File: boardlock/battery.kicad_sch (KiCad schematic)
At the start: 20 parts, among them J1 Conn_01x02, J2 Conn_01x02, U4 BQ27441DRZR-G1A, U5 BQ24075RGT

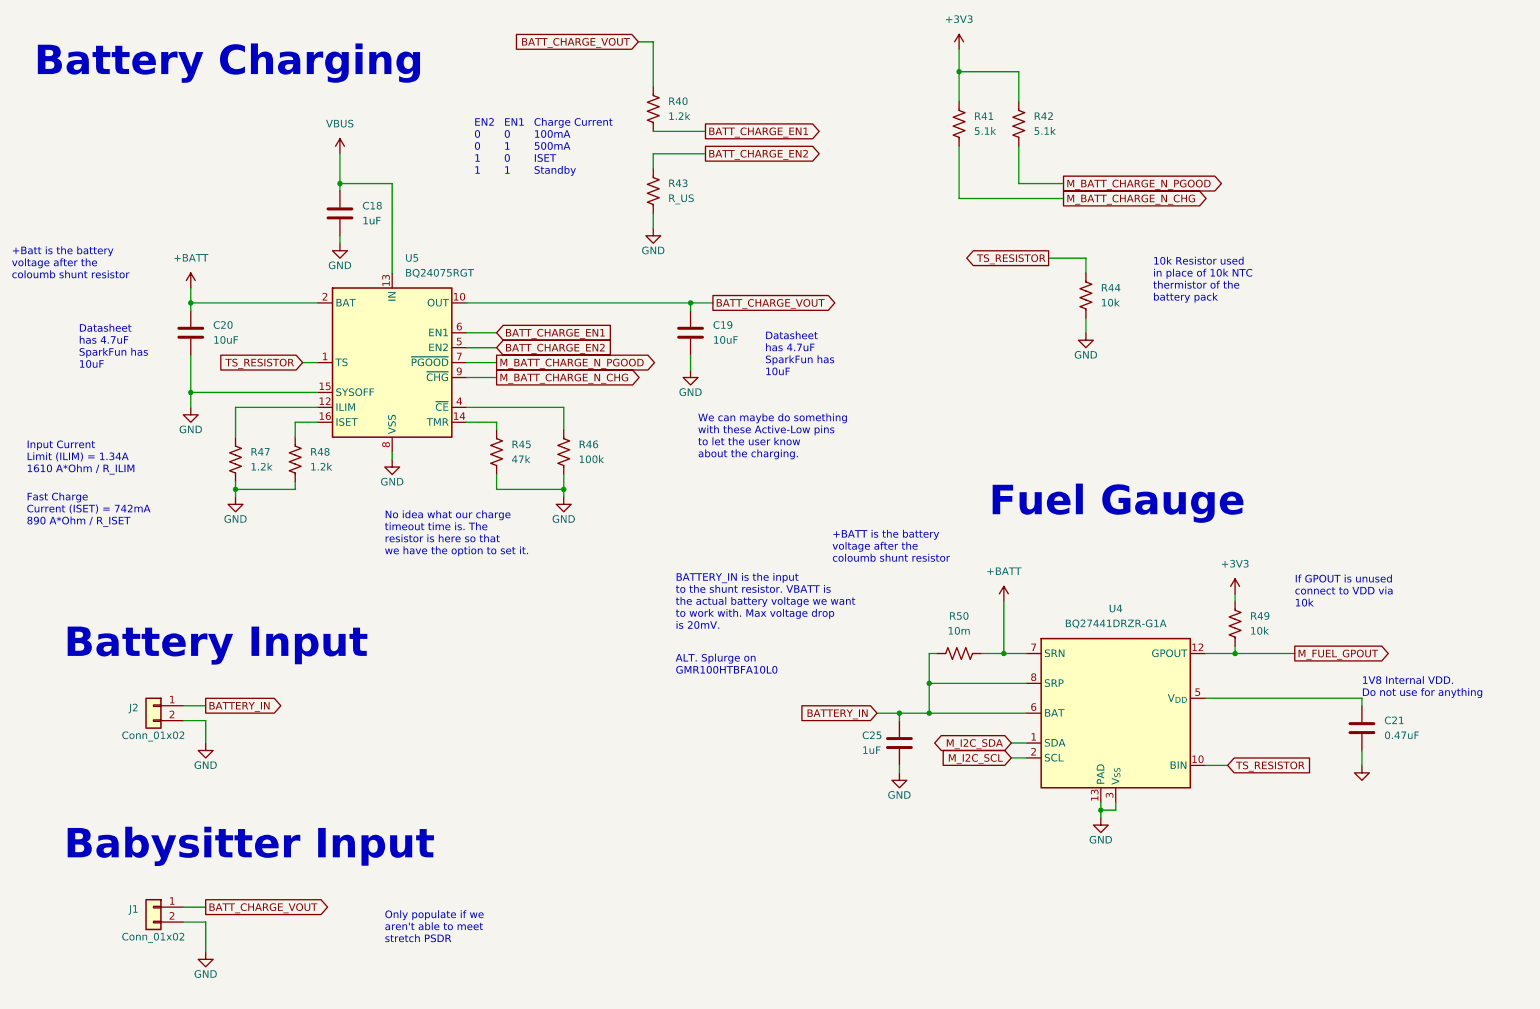
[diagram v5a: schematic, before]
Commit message: Repositioned USB C port
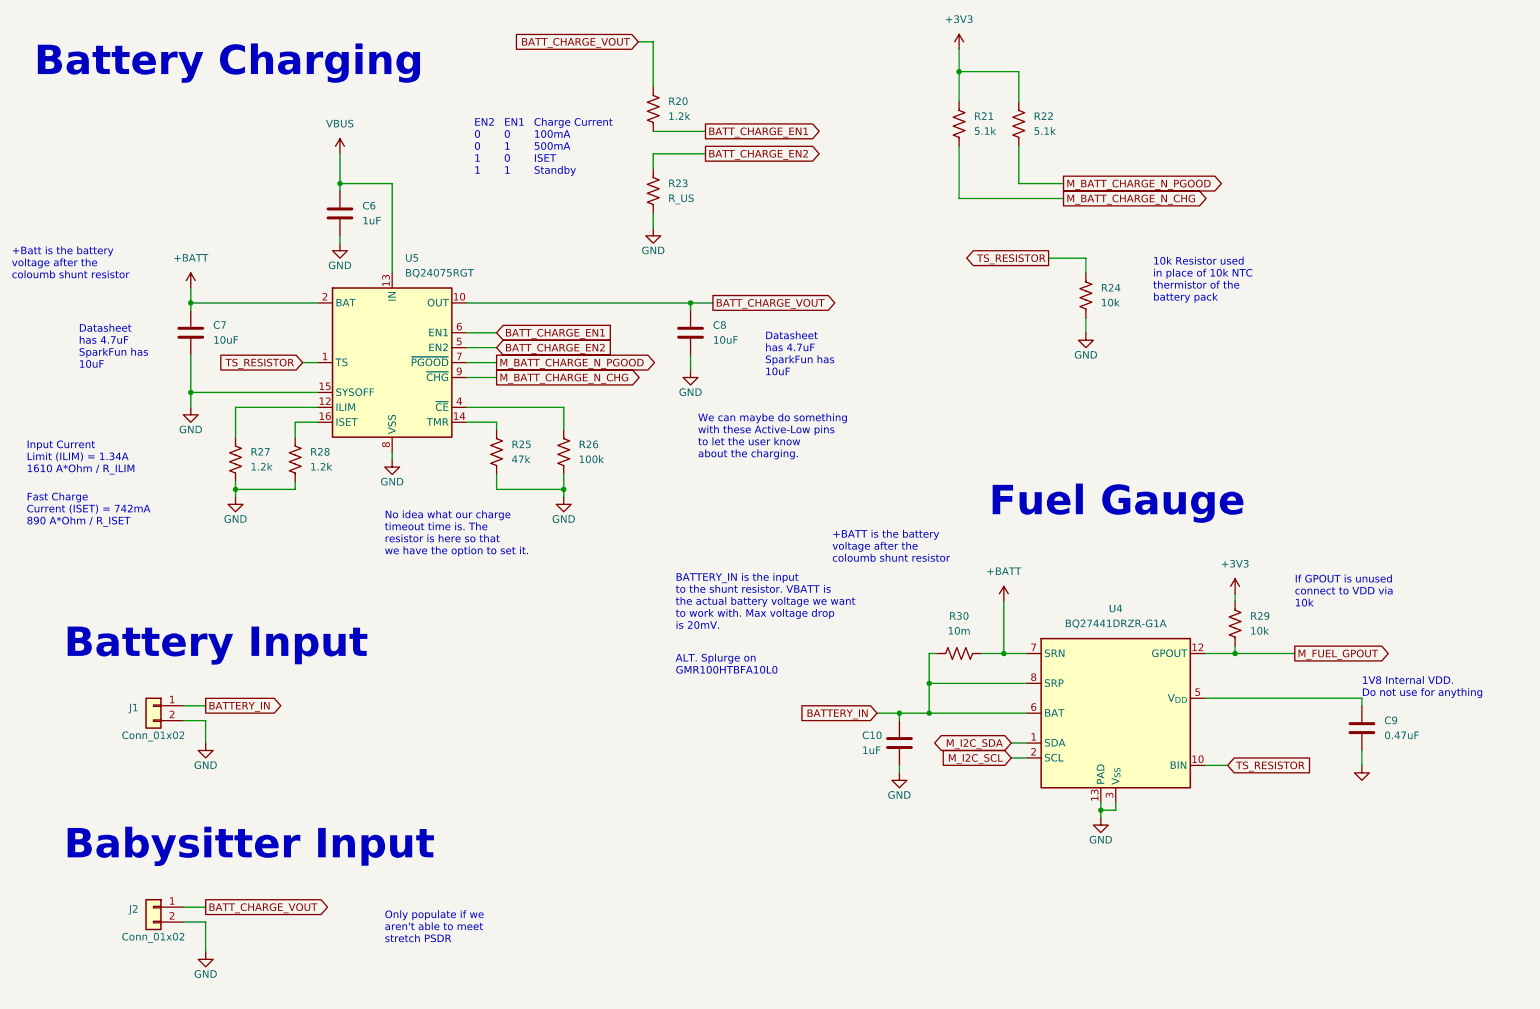
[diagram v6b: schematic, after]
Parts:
- renumbered C25 to C10, C18 to C6, C20 to C7, C19 to C8, C21 to C9, J2 to J1, J1 to J2, R40 to R20, R41 to R21, R42 to R22, R43 to R23, R44 to R24, R45 to R25, R46 to R26, R47 to R27, R48 to R28, R49 to R29, R50 to R30

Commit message: USB traces
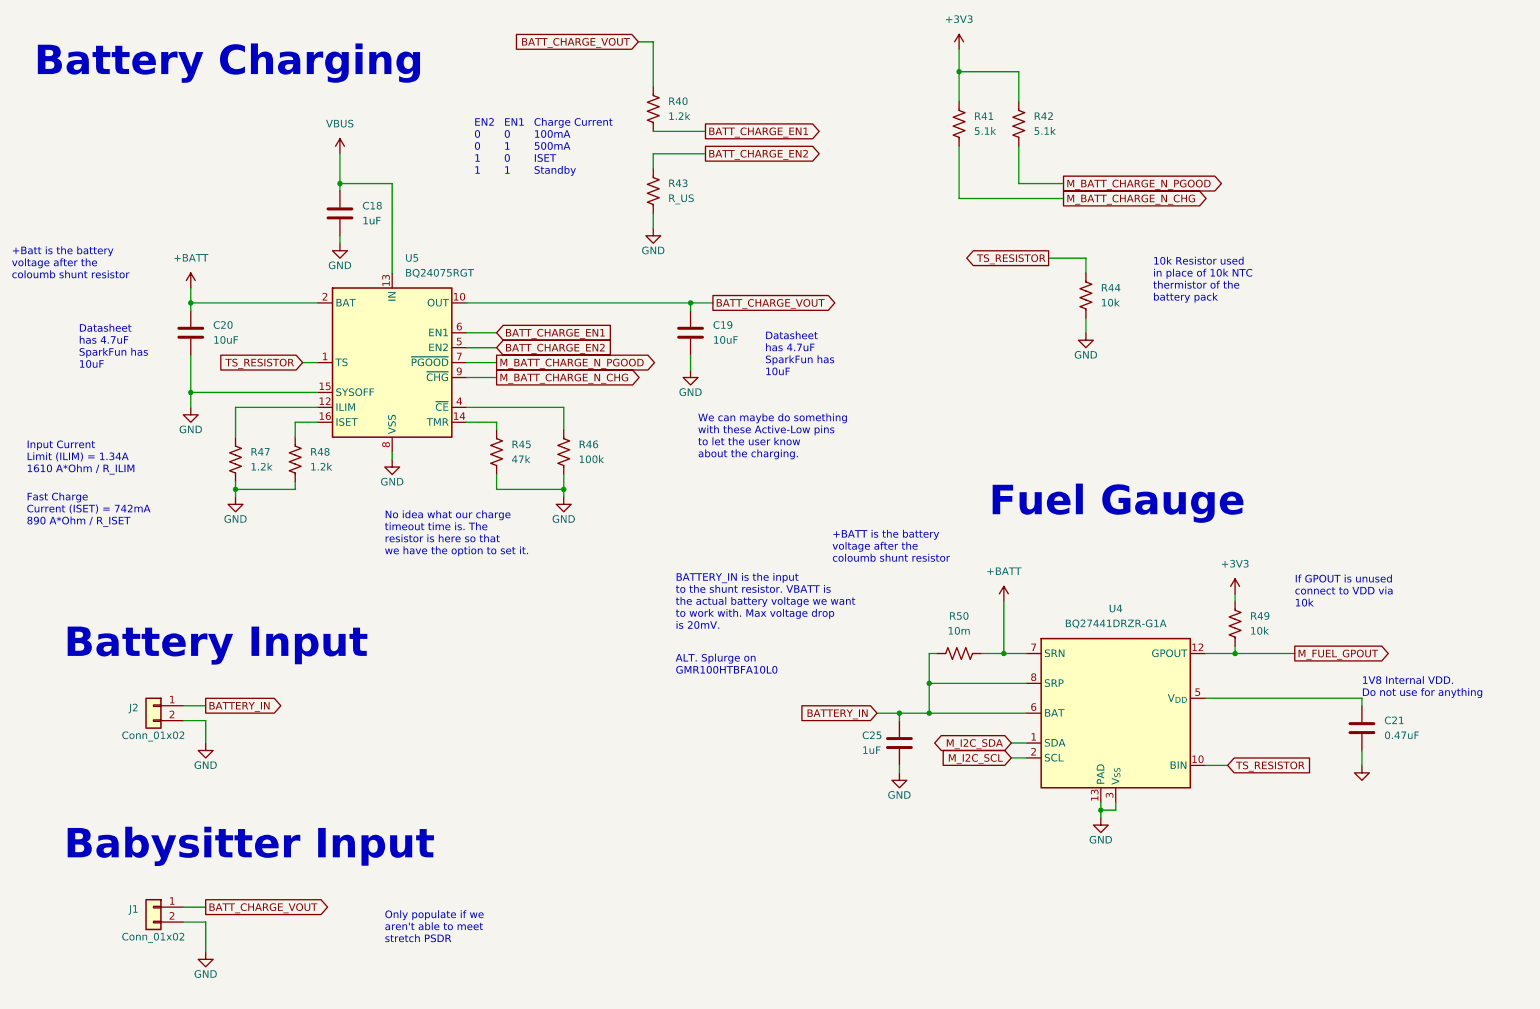
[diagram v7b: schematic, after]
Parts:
- C18: renamed from C6; footprint Capacitor_SMD:C_0805_2012Metric_Pad1.18x1.45mm_HandSolder -> Capacitor_SMD:C_0603_1608Metric_Pad1.08x0.95mm_HandSolder
- C19: renamed from C8; footprint Capacitor_SMD:C_0805_2012Metric_Pad1.18x1.45mm_HandSolder -> Capacitor_SMD:C_0603_1608Metric_Pad1.08x0.95mm_HandSolder
- renumbered C7 to C20, C9 to C21, C10 to C25, J2 to J1, J1 to J2, R20 to R40, R21 to R41, R22 to R42, R23 to R43, R24 to R44, R25 to R45, R26 to R46, R27 to R47, R28 to R48, R29 to R49, R30 to R50

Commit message: more pcb stuff
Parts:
- renumbered C25 to C10, C18 to C6, C20 to C7, C19 to C8, C21 to C9, J2 to J1, J1 to J2, R40 to R15, R41 to R16, R42 to R17, R43 to R18, R44 to R19, R45 to R20, R46 to R21, R47 to R22, R48 to R23, R49 to R24, R50 to R25
